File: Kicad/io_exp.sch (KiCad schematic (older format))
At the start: 4 parts, among them U1001 MCP23S17_SO, U1002 74HC245

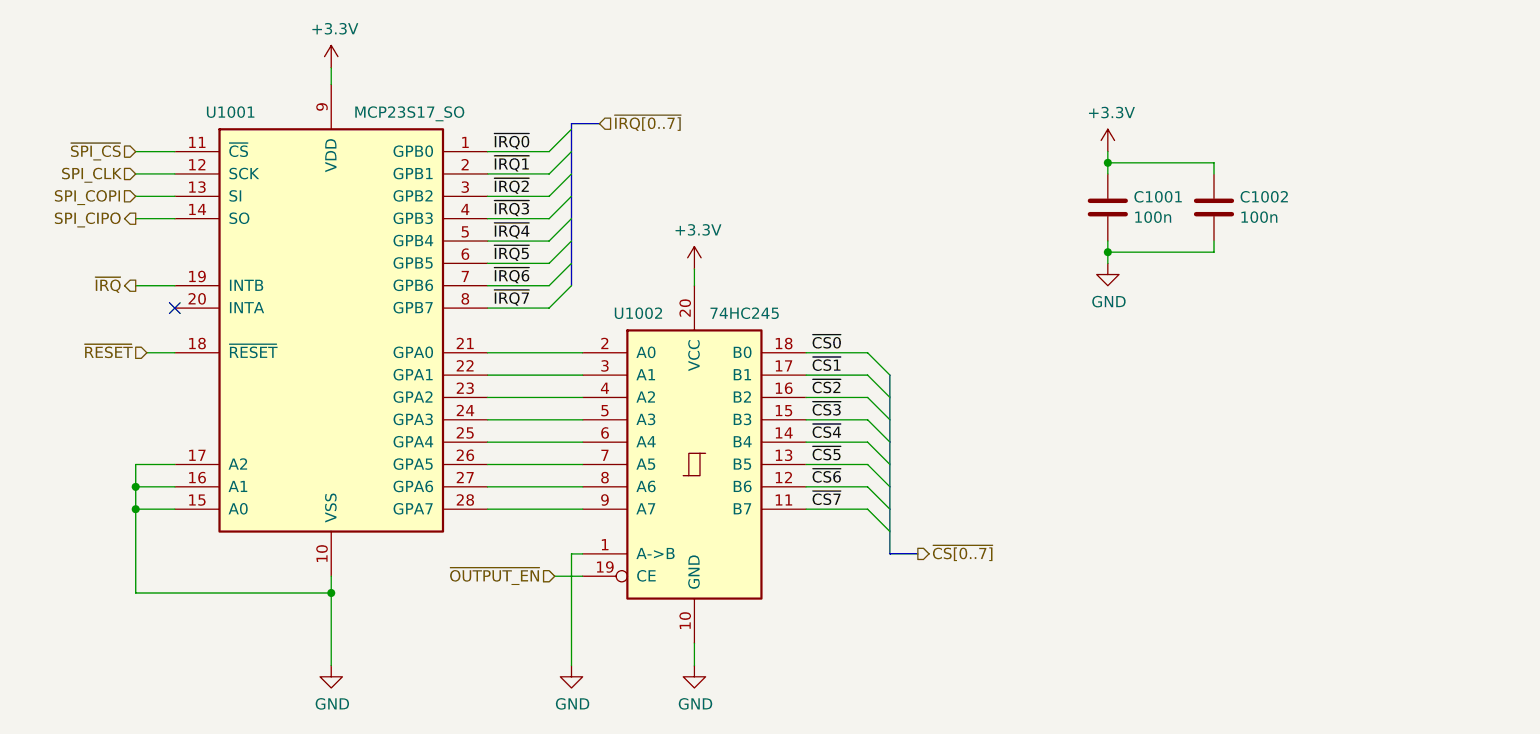
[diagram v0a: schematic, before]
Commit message: Tidy-ups.
) Rewired audio block to pico
) Clarified meaning of USB power jumper and gave better
warning about not plugging in power when jumper fitted.
) We can refer to components now our sheet numbers don't change - note
Q801 on powersupply sheet
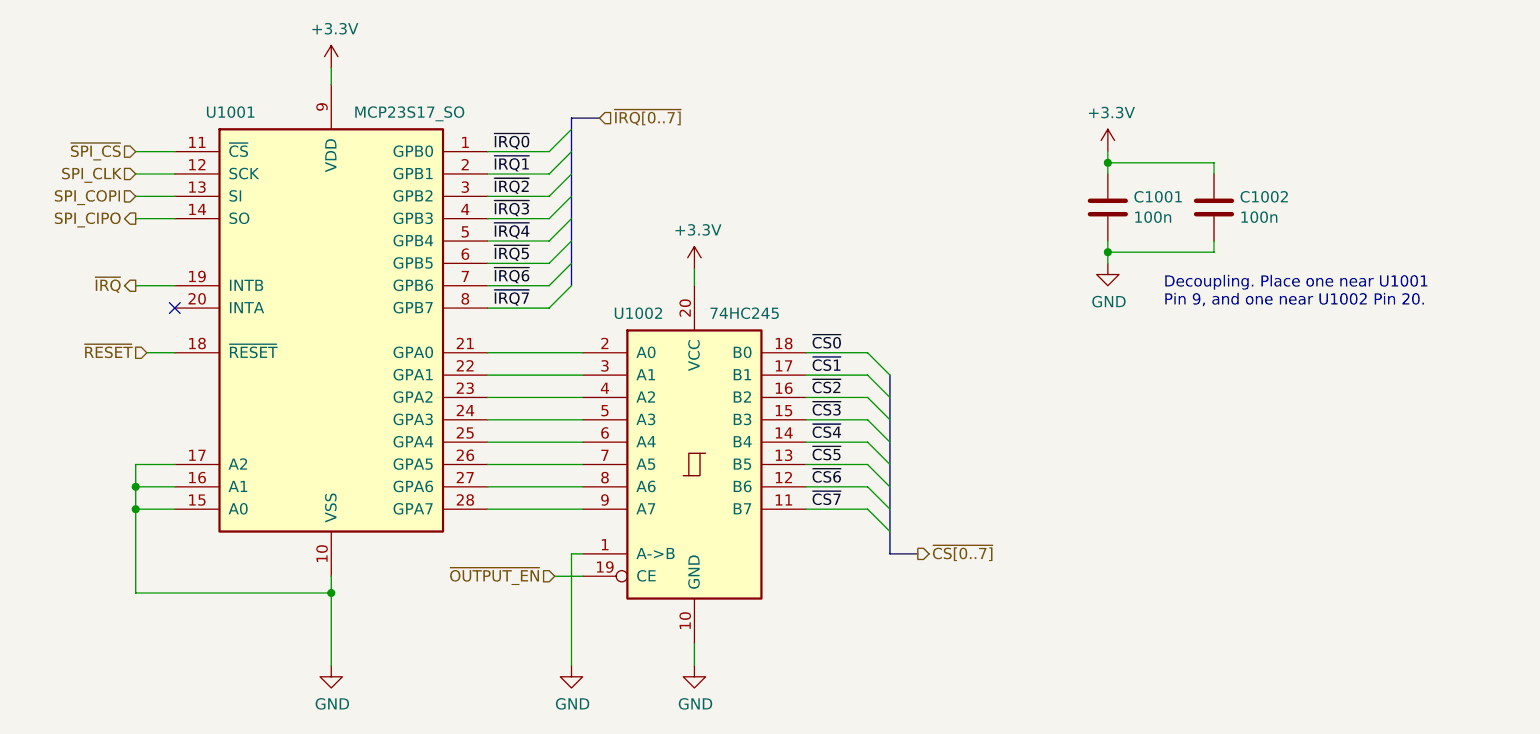
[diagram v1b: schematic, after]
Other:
- note added: "Decoupling. Place one near U1001\nPin 9, and one near U1002 Pin 20."
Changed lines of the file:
@@
 Wire Bus Line
 	6925 4050 7050 4050
-Text HLabel 5625 2125 2    50   Input ~ 0
+Text HLabel 5625 2100 2    50   Input ~ 0
 ~IRQ[0..7]
 Entry Wire Line
@@
 ~IRQ7
 Wire Bus Line
-	5500 2125 5625 2125
+	5500 2100 5625 2100
 $Comp
 L 74xx:74HC245 U1002
@@
 Wire Wire Line
 	7900 2700 7900 2750
-Wire Bus Line
-	5500 2125 5500 2850
+Text Notes 8150 2950 0    50   ~ 0
+Decoupling. Place one near U1001\nPin 9, and one near U1002 Pin 20.
+Wire Bus Line
+	5500 2100 5500 2850
 Wire Bus Line
 	6925 3250 6925 4050

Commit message: Switching some parts over to the CPL.
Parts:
- C1001, C1002: Digikey BC1150CT-ND -> (none); MPN K104K15X7RF5TL2 -> CPL-CAP-X7R-0805-100NF-50V; Manufacturer Vishay -> CPL; Mouser 594-K104K15X7RF5TL2 -> (none)
- U1001: DNP (none) -> 0; Digikey (none) -> MCP23S17T-E/SOCT-ND; MPN (none) -> MCP23S17T-E/SO; Manufacturer (none) -> Microchip
- U1002: DNP (none) -> 0; Digikey (none) -> 296-8278-1-ND; MPN (none) -> SN74HC245NSR; Manufacturer (none) -> Texas Instruments
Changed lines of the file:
@@
 F 2 "Package_SO:SOIC-28W_7.5x17.9mm_P1.27mm" H 4625 2050 50  0001 L CNN
 F 3 "http://ww1.microchip.com/downloads/en/DeviceDoc/20001952C.pdf" H 4625 1950 50  0001 L CNN
+F 4 "0" H 4425 3050 50  0001 C CNN "DNP"
+F 5 "MCP23S17T-E/SOCT-ND" H 4425 3050 50  0001 C CNN "Digikey"
+F 6 "MCP23S17T-E/SO" H 4425 3050 50  0001 C CNN "MPN"
+F 7 "Microchip" H 4425 3050 50  0001 C CNN "Manufacturer"
 	1    4425 3050
 	1    0    0    -1
@@
 F 2 "Package_SO:SO-20_12.8x7.5mm_P1.27mm" H 6050 3650 50  0001 C CNN
 F 3 "http://www.ti.com/lit/gpn/sn74HC245" H 6050 3650 50  0001 C CNN
+F 4 "0" H 6050 3650 50  0001 C CNN "DNP"
+F 5 "296-8278-1-ND" H 6050 3650 50  0001 C CNN "Digikey"
+F 6 "SN74HC245NSR" H 6050 3650 50  0001 C CNN "MPN"
+F 7 "Texas Instruments" H 6050 3650 50  0001 C CNN "Manufacturer"
 	1    6050 3650
 	1    0    0    -1
@@
 F 3 "~" H 7900 2500 50  0001 C CNN
 F 4 "0" H 7900 2500 50  0001 C CNN "DNP"
-F 5 "BC1150CT-ND" H 7900 2500 50  0001 C CNN "Digikey"
-F 6 "K104K15X7RF5TL2" H 7900 2500 50  0001 C CNN "MPN"
-F 7 "Vishay" H 7900 2500 50  0001 C CNN "Manufacturer"
-F 8 "594-K104K15X7RF5TL2" H 7900 2500 50  0001 C CNN "Mouser"
+F 5 "" H 7900 2500 50  0001 C CNN "Digikey"
+F 6 "CPL-CAP-X7R-0805-100NF-50V" H 7900 2500 50  0001 C CNN "MPN"
+F 7 "CPL" H 7900 2500 50  0001 C CNN "Manufacturer"
+F 8 "" H 7900 2500 50  0001 C CNN "Mouser"
 	1    7900 2500
 	1    0    0    -1
@@
 F 3 "~" H 8375 2500 50  0001 C CNN
 F 4 "0" H 8375 2500 50  0001 C CNN "DNP"
-F 5 "BC1150CT-ND" H 8375 2500 50  0001 C CNN "Digikey"
-F 6 "K104K15X7RF5TL2" H 8375 2500 50  0001 C CNN "MPN"
-F 7 "Vishay" H 8375 2500 50  0001 C CNN "Manufacturer"
-F 8 "594-K104K15X7RF5TL2" H 8375 2500 50  0001 C CNN "Mouser"
+F 5 "" H 8375 2500 50  0001 C CNN "Digikey"
+F 6 "CPL-CAP-X7R-0805-100NF-50V" H 8375 2500 50  0001 C CNN "MPN"
+F 7 "CPL" H 8375 2500 50  0001 C CNN "Manufacturer"
+F 8 "" H 8375 2500 50  0001 C CNN "Mouser"
 	1    8375 2500
 	1    0    0    -1

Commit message: Fixing some review comments.
* PCB has rounded corners.
* Add JLCPCB part numbers for SMT parts
* Fixed Fab layer
* Renumbered Slots
* Mounting holes do not have thermal relief

Closes #13 #12 and #10
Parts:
- C1001, C1002: LCSC Part# (none) -> C49678
- U1001: LCSC Part# (none) -> C145413
- U1002: LCSC Part# (none) -> C5625
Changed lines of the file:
@@
 F 6 "MCP23S17T-E/SO" H 4425 3050 50  0001 C CNN "MPN"
 F 7 "Microchip" H 4425 3050 50  0001 C CNN "Manufacturer"
+F 8 "C145413" H 4425 3050 50  0001 C CNN "LCSC Part#"
 	1    4425 3050
 	1    0    0    -1
@@
 F 6 "SN74HC245NSR" H 6050 3650 50  0001 C CNN "MPN"
 F 7 "Texas Instruments" H 6050 3650 50  0001 C CNN "Manufacturer"
+F 8 "C5625" H 6050 3650 50  0001 C CNN "LCSC Part#"
 	1    6050 3650
 	1    0    0    -1
@@
 F 7 "CPL" H 7900 2500 50  0001 C CNN "Manufacturer"
 F 8 "" H 7900 2500 50  0001 C CNN "Mouser"
+F 9 "C49678" H 7900 2500 50  0001 C CNN "LCSC Part#"
 	1    7900 2500
 	1    0    0    -1
@@
 F 7 "CPL" H 8375 2500 50  0001 C CNN "Manufacturer"
 F 8 "" H 8375 2500 50  0001 C CNN "Mouser"
+F 9 "C49678" H 8375 2500 50  0001 C CNN "LCSC Part#"
 	1    8375 2500
 	1    0    0    -1

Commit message: BoM and PCB fixes.
* Move tolerances and voltages out of value and into their own fields.
* Fix 5V trace for audio stage.
* Fixup docs.yml so outputs work for JLCPCB.
* Fix JLCPCB part number for 22pF caps.
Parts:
- C1001, C1002: value 100n -> 100nF
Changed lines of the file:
@@
 AR Path="/6069D32A/60F34F63" Ref="C1001"  Part="1"
 F 0 "C1001" H 8015 2546 50  0000 L CNN
-F 1 "100n" H 8015 2455 50  0000 L CNN
+F 1 "100nF" H 8015 2455 50  0000 L CNN
 F 2 "Capacitor_SMD:C_0805_2012Metric_Pad1.18x1.45mm_HandSolder" H 7938 2350 50  0001 C CNN
 F 3 "~" H 7900 2500 50  0001 C CNN
@@
 AR Path="/6069D32A/60F36BE4" Ref="C1002"  Part="1"
 F 0 "C1002" H 8490 2546 50  0000 L CNN
-F 1 "100n" H 8490 2455 50  0000 L CNN
+F 1 "100nF" H 8490 2455 50  0000 L CNN
 F 2 "Capacitor_SMD:C_0805_2012Metric_Pad1.18x1.45mm_HandSolder" H 8413 2350 50  0001 C CNN
 F 3 "~" H 8375 2500 50  0001 C CNN

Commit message: Update component values.
Tolerance and Voltage are set to the minimum acceptable. The selected
parts can be better, where a better part is cheaper or has
better availability.

Also dropped R2R DAC tolerance to 1% - 0.5% was overkill. The output
resistor had the wrong value too, which is fixed.
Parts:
- C1001, C1002: Tolerance (none) -> X5R; Voltage (none) -> 50V
- U1002: Mouser (none) -> 595-SN74HC245NSR
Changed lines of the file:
@@
 F 7 "Microchip" H 4425 3050 50  0001 C CNN "Manufacturer"
 F 8 "C145413" H 4425 3050 50  0001 C CNN "LCSC Part#"
+F 9 "~" H 4425 3050 50  0001 C CNN "Mouser"
+F 10 "~" H 4425 3050 50  0001 C CNN "Tolerance"
+F 11 "~" H 4425 3050 50  0001 C CNN "Voltage"
 	1    4425 3050
 	1    0    0    -1
@@
 F 7 "Texas Instruments" H 6050 3650 50  0001 C CNN "Manufacturer"
 F 8 "C5625" H 6050 3650 50  0001 C CNN "LCSC Part#"
+F 9 "595-SN74HC245NSR" H 6050 3650 50  0001 C CNN "Mouser"
+F 10 "~" H 6050 3650 50  0001 C CNN "Tolerance"
+F 11 "~" H 6050 3650 50  0001 C CNN "Voltage"
 	1    6050 3650
 	1    0    0    -1
@@
 F 3 "~" H 7900 2500 50  0001 C CNN
 F 4 "0" H 7900 2500 50  0001 C CNN "DNP"
-F 5 "" H 7900 2500 50  0001 C CNN "Digikey"
+F 5 "~" H 7900 2500 50  0001 C CNN "Digikey"
 F 6 "CPL-CAP-X7R-0805-100NF-50V" H 7900 2500 50  0001 C CNN "MPN"
 F 7 "CPL" H 7900 2500 50  0001 C CNN "Manufacturer"
-F 8 "" H 7900 2500 50  0001 C CNN "Mouser"
+F 8 "~" H 7900 2500 50  0001 C CNN "Mouser"
 F 9 "C49678" H 7900 2500 50  0001 C CNN "LCSC Part#"
+F 10 "X5R" H 7900 2500 50  0001 C CNN "Tolerance"
+F 11 "50V" H 7900 2500 50  0001 C CNN "Voltage"
 	1    7900 2500
 	1    0    0    -1
@@
 F 3 "~" H 8375 2500 50  0001 C CNN
 F 4 "0" H 8375 2500 50  0001 C CNN "DNP"
-F 5 "" H 8375 2500 50  0001 C CNN "Digikey"
+F 5 "~" H 8375 2500 50  0001 C CNN "Digikey"
 F 6 "CPL-CAP-X7R-0805-100NF-50V" H 8375 2500 50  0001 C CNN "MPN"
 F 7 "CPL" H 8375 2500 50  0001 C CNN "Manufacturer"
-F 8 "" H 8375 2500 50  0001 C CNN "Mouser"
+F 8 "~" H 8375 2500 50  0001 C CNN "Mouser"
 F 9 "C49678" H 8375 2500 50  0001 C CNN "LCSC Part#"
+F 10 "X5R" H 8375 2500 50  0001 C CNN "Tolerance"
+F 11 "50V" H 8375 2500 50  0001 C CNN "Voltage"
 	1    8375 2500
 	1    0    0    -1

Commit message: Drop capacitor voltage ratings where possible.
Audio circuit is 1V RMS, so 6.3V is fine.
Use 10V for 3.3V circuits.
Use 16V for 5.0V circuits.
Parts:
- C1001, C1002: Voltage 50V -> 10V
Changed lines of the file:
@@
 F 9 "C49678" H 7900 2500 50  0001 C CNN "LCSC Part#"
 F 10 "X5R" H 7900 2500 50  0001 C CNN "Tolerance"
-F 11 "50V" H 7900 2500 50  0001 C CNN "Voltage"
+F 11 "10V" H 7900 2500 50  0001 C CNN "Voltage"
 	1    7900 2500
 	1    0    0    -1
@@
 F 9 "C49678" H 8375 2500 50  0001 C CNN "LCSC Part#"
 F 10 "X5R" H 8375 2500 50  0001 C CNN "Tolerance"
-F 11 "50V" H 8375 2500 50  0001 C CNN "Voltage"
+F 11 "10V" H 8375 2500 50  0001 C CNN "Voltage"
 	1    8375 2500
 	1    0    0    -1
